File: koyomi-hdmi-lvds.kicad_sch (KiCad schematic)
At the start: 41 parts, among them IC1 SN75LVDS83B, J1 20374-R30E-31, J2 HDMI_I2C, J3 I/O, U1 TFP401, U2 24LC02B, U3 AP2114H-2.5

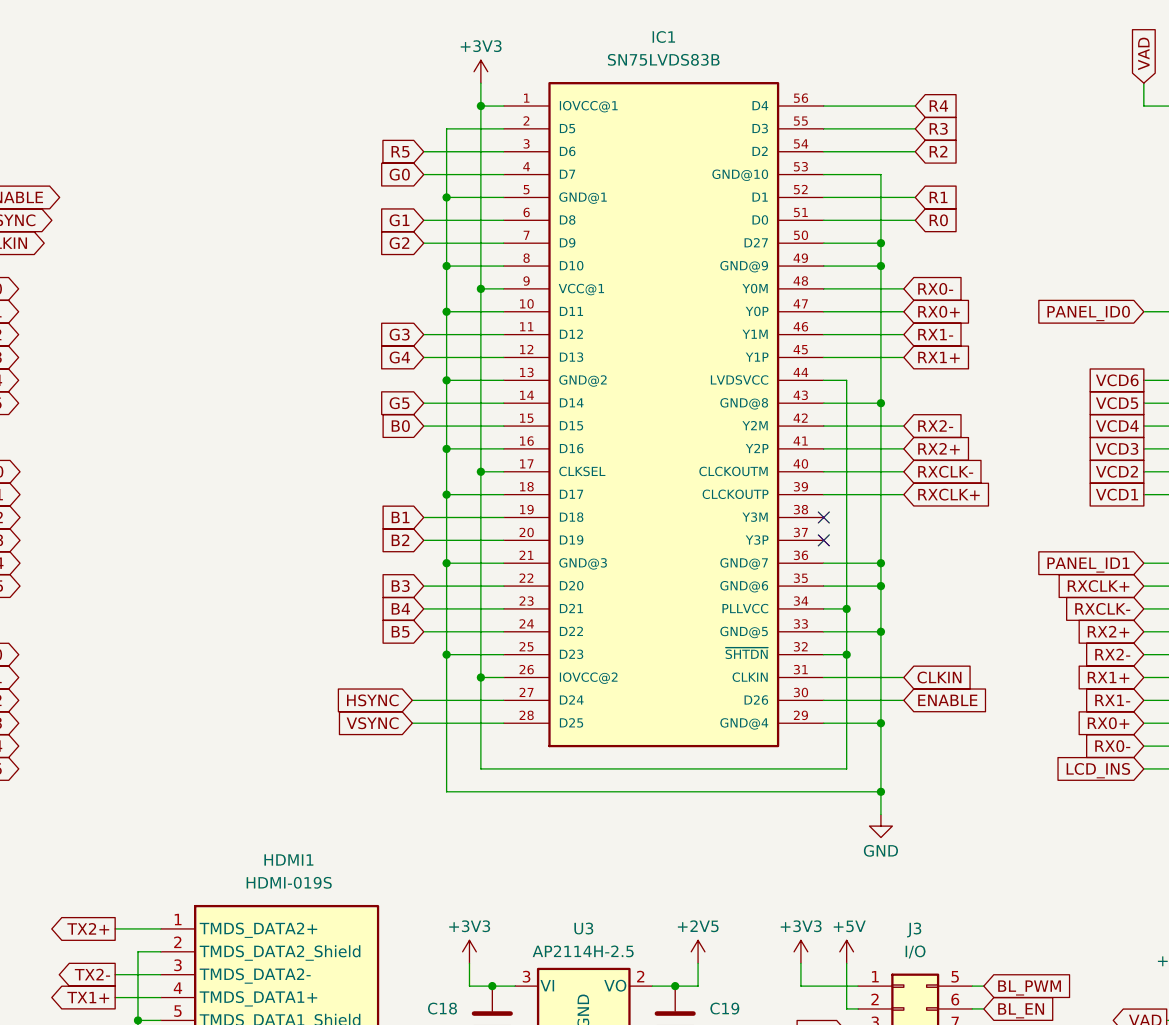
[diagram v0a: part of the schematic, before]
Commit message: v1.1: added LVDS common mode filters, JLCPCB CPL fixes
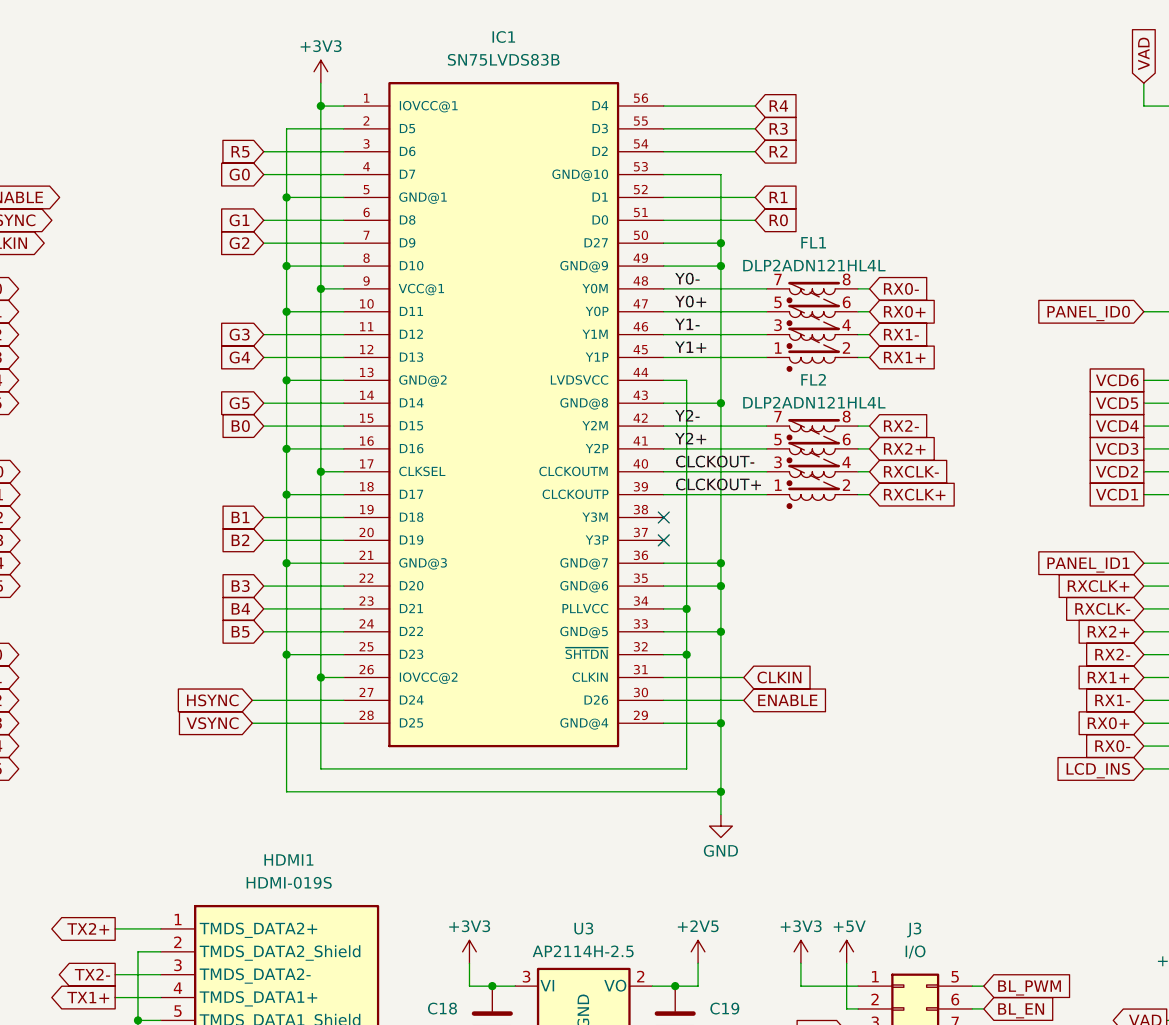
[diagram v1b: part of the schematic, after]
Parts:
- added FL1, FL2: DLP2ADN121HL4L, Murata_DLP2ADN121HL4L:Murata_DLP2ADN121HL4L, symbol Device:Filter_EMI_LLLL
- C1, C10, C11, C12, C13, C2, C21, C24, C3, C4, C5, C6, C7, C8, C9: LCSC (none) -> C1591
- C14, C15, C16, C17: LCSC (none) -> C86295
- C18, C19: LCSC (none) -> C1705
- C20, C23: LCSC (none) -> C1592
- C22, C25: LCSC (none) -> C1589
- FB1, FB2, FB3, FB4: LCSC (none) -> C19330
- HDMI1: LCSC (none) -> C111617
- IC1: LCSC (none) -> C35164
- R1, R2, R3: LCSC (none) -> C844791
- U1: LCSC (none) -> C962083
- U2: LCSC (none) -> C2987265
- U3: LCSC (none) -> C460313
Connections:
- net RX0+: now also FL1.6; no longer IC1.47 (Y0P)
- net RX0-: now also FL1.8; no longer IC1.48 (Y0M)
- net RX1+: now also FL1.2; no longer IC1.45 (Y1P)
- net RX1-: now also FL1.4; no longer IC1.46 (Y1M)
- net RX2+: now also FL2.6; no longer IC1.41 (Y2P)
- net RX2-: now also FL2.8; no longer IC1.42 (Y2M)
- net RXCLK+: now also FL2.2; no longer IC1.39 (CLCKOUTP)
- net RXCLK-: now also FL2.4; no longer IC1.40 (CLCKOUTM)
- new net CLCKOUT+: FL2.1, IC1.39 (CLCKOUTP)
- new net CLCKOUT-: FL2.3, IC1.40 (CLCKOUTM)
- new net Y0+: FL1.5, IC1.47 (Y0P)
- new net Y0-: FL1.7, IC1.48 (Y0M)
- new net Y1+: FL1.1, IC1.45 (Y1P)
- new net Y1-: FL1.3, IC1.46 (Y1M)
- new net Y2+: FL2.5, IC1.41 (Y2P)
- new net Y2-: FL2.7, IC1.42 (Y2M)
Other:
- moved on the sheet: IC1

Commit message: Murata DLP2ADN121HL4L footprint cleanup
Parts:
- J2, J3: now left out of the parts list
- J4: value ~ -> (none); now left out of the parts list
